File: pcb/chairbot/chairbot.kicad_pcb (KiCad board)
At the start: 2 copper layers, 66.9 x 100 mm, 35 parts, among them J1 Conn_01x02, J2 Conn_01x05, J3 Conn_01x02, J4 Conn_01x07, J5 Conn_01x07, Q1 ZXMN4A06G, U1 ESP32mini, U2 74HCT08, U3 74HCT244, U4 buck-converter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

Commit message: Fix various issues.
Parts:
- removed F1: Fuse, Resistor_THT:R_Axial_DIN0309_L9.0mm_D3.2mm_P2.54mm_Vertical
- added C11: 100n, Capacitor_SMD:C_0603_1608Metric, F.Cu at (71.8, 137.8)
- added R3: 10K, Resistor_SMD:R_0603_1608Metric, F.Cu at (56.5, 151.1)
- added R4: 1K, Resistor_SMD:R_0603_1608Metric, F.Cu at (71.8, 141.0)
- added R5: 2K2, Resistor_SMD:R_0603_1608Metric, F.Cu at (59.1, 90.8)
- added REF**: MountingHole_3.2mm_M3, MountingHole:MountingHole_3.2mm_M3, F.Cu at (97.2, 138.7)
- moved D1 11.9 mm to (51.2, 176.5), turned to 0 degrees
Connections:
- D1 pad 2: GND -> Net-(D1-Pad2)
- J1 pad 2: Net-(F1-Pad2) -> Net-(D1-Pad2)
- J4 pad 6: (no net) -> Net-(J4-Pad6)
- J5 pad 6: (no net) -> Net-(J5-Pad6)
- U1 pad 13: (no net) -> Net-(U1-Pad13)
- U1 pad 15: (no net) -> Net-(U1-Pad15)
- U1 pad 17: (no net) -> Net-(U1-Pad17)
- U1 pad 18: (no net) -> Net-(U1-Pad18)
- U1 pad 19: (no net) -> Net-(U1-Pad19)
- U1 pad 2: (no net) -> Net-(U1-Pad2)
- U1 pad 20: (no net) -> Net-(U1-Pad20)
- U1 pad 21: (no net) -> Brake
- U1 pad 23: (no net) -> Net-(U1-Pad23)
- U1 pad 24: (no net) -> MISO
- U1 pad 26: Brake -> Vbat
- U1 pad 3: (no net) -> Net-(U1-Pad3)
- U1 pad 34: MISO -> Net-(U1-Pad34)
- U1 pad 37: (no net) -> Net-(U1-Pad37)
- U1 pad 38: (no net) -> Net-(U1-Pad38)
- U1 pad 39: (no net) -> Net-(U1-Pad39)
- U1 pad 4: (no net) -> Net-(U1-Pad4)
- U1 pad 40: (no net) -> Net-(U1-Pad40)
- U1 pad 5: (no net) -> Net-(U1-Pad5)
- U2 pad 11: (no net) -> Net-(U2-Pad11)
- U2 pad 6: (no net) -> Net-(U2-Pad6)
- U2 pad 8: (no net) -> Net-(U2-Pad8)
- U3 pad 3: (no net) -> Net-(U3-Pad3)
- U3 pad 5: (no net) -> Net-(U3-Pad5)
- U3 pad 7: (no net) -> Net-(U3-Pad7)
- U3 pad 9: (no net) -> Net-(U3-Pad9)
- U5 pad 8: (no net) -> Net-(U5-Pad8)
- U9 pad 5: (no net) -> Net-(U9-Pad5)
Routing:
- net Vbat: track 0.00 -> 85.8 mm, vias 0 -> 5
- net MISO: track 51.3 -> 79.2 mm, vias 0 -> 1
- net Net-(F1-Pad2): track 11.8 -> 0.00 mm
- net Net-(D1-Pad2): track 0.00 -> 7.44 mm
- net +5V: track 250.2 -> 253.9 mm
- net GND: track 364.2 -> 366.8 mm
- net Brake: track 148.3 -> 145.8 mm
- net EN: track 20.6 -> 22.9 mm
- net +24V: track 79.5 -> 77.5 mm

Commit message: Fix more stuff.
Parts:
- moved R1 1.27 mm to (77.5, 177.8)
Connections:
- Q1 pad 1: Net-(D2-Pad2) -> Net-(Q1-Pad1)
- Q1 pad 2: Net-(Q1-Pad2) -> Net-(D2-Pad2)
- R1 pad 1: Net-(Q1-Pad2) -> Net-(Q1-Pad1)
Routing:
- net Net-(Q1-Pad1): track 0.00 -> 8.70 mm, vias 0 -> 2
- net Net-(Q1-Pad2): track 7.62 -> 0.00 mm
- net GND: track 366.8 -> 364.3 mm
- net Net-(D2-Pad2): track 32.3 -> 30.3 mm
- net Brake: track 145.8 -> 144.5 mm
- added copper zone on F.Cu, net GND

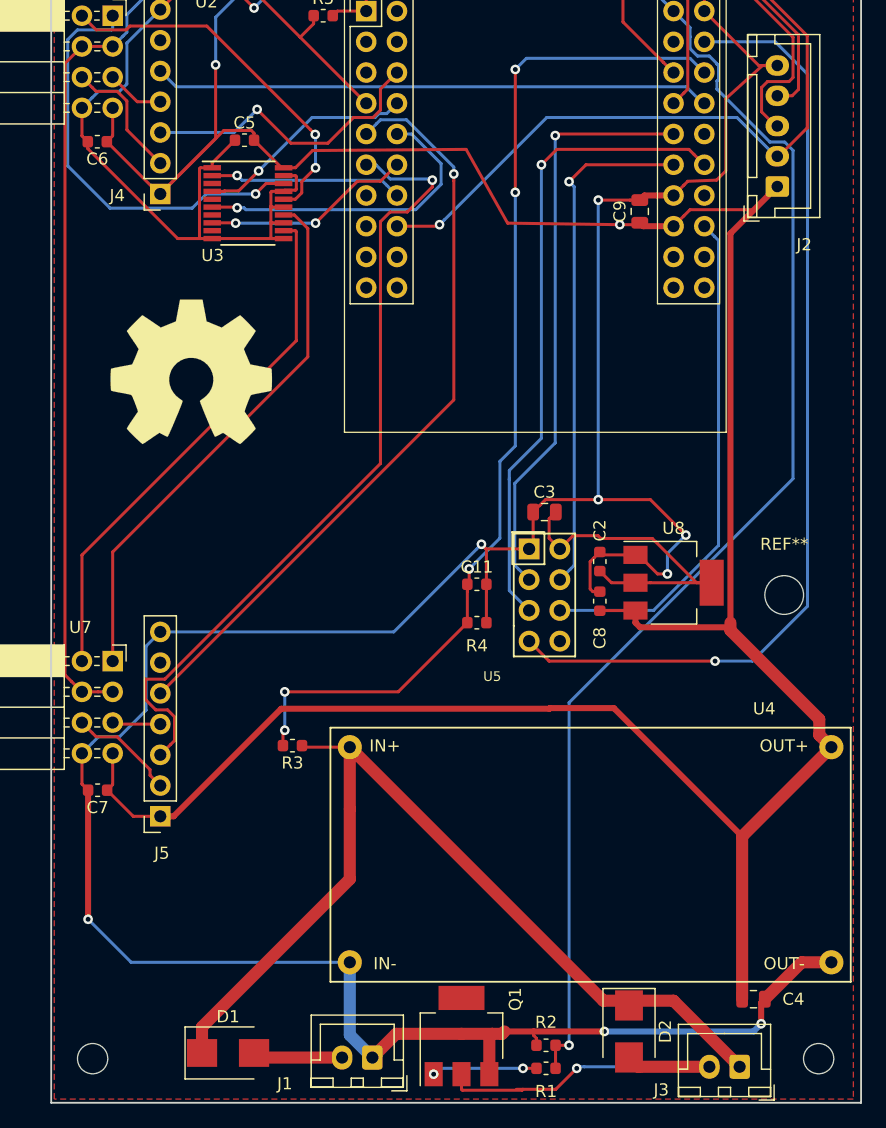
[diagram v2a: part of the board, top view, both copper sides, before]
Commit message: Tweak pin numbers.
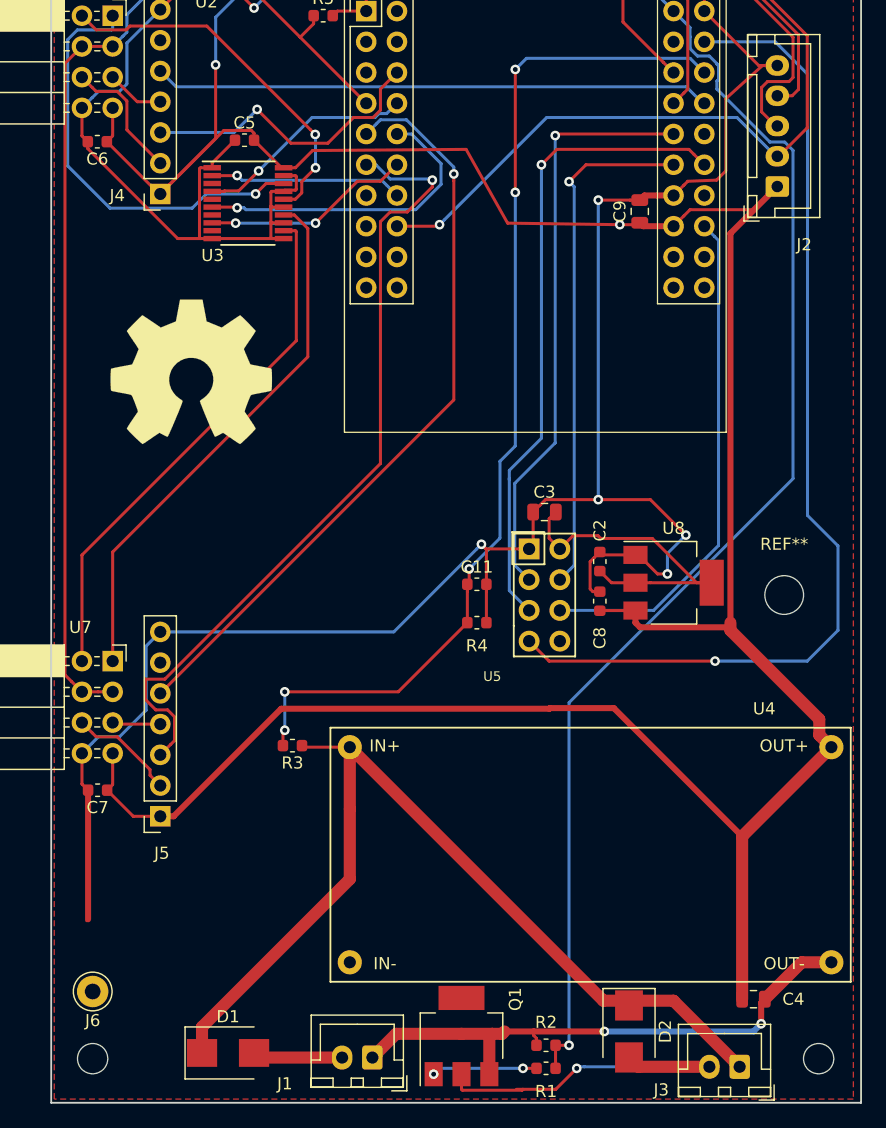
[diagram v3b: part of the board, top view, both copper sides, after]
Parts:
- added J6: GND, Connector_Pin:Pin_D1.3mm_L11.0mm, F.Cu at (40.0, 171.4)
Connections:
- R1 pad 2: Brake -> EN
- R2 pad 2: Brake -> EN
- U1 pad 21: Brake -> Net-(U1-Pad21)
- U1 pad 26: Vbat -> EN
- U1 pad 7: EN -> Vbat
- U2 pad 2: Brake -> EN
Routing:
- net GND: track 364.3 -> 332.5 mm, vias 8 -> 7
- net MISO: track 79.2 -> 83.9 mm
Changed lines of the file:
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@@
-(kicad_pcb (version 20171130) (host pcbnew 5.0.2-bee76a0~70~ubuntu18.04.1)
+(kicad_pcb (version 20171130) (host pcbnew 5.1.2-f72e74a~84~ubuntu18.04.1)
   (general
     (thickness 1.6)
     (drawings 5)
-    (tracks 550)
+    (tracks 547)
     (zones 0)
-    (modules 39)
-    (nets 65)
+    (modules 40)
+    (nets 66)
   )
   (page A4)
   (layers
-    (0 F.Cu signal)
+    (0 F.Cu signal hide)
     (31 B.Cu signal)
     (32 B.Adhes user)
@@
   )
   (setup
-    (last_trace_width 1)
+    (last_trace_width 0.25)
     (user_trace_width 0.5)
     (user_trace_width 1)
@@
     (zone_45_only no)
     (trace_min 0.2)
-    (segment_width 0.2)
-    (edge_width 0.15)
     (via_size 0.8)
     (via_drill 0.4)
@@
     (uvia_min_size 0.2)
     (uvia_min_drill 0.1)
+    (edge_width 0.15)
+    (segment_width 0.2)
     (pcb_text_width 0.3)
     (pcb_text_size 1.5 1.5)
@@
       (padsonsilk false)
       (subtractmaskfromsilk false)
-      (outputformat 5)
+      (outputformat 1)
       (mirror false)
       (drillshape 0)
@@
   (net 63 "Net-(D1-Pad2)")
   (net 64 "Net-(Q1-Pad1)")
+  (net 65 "Net-(U1-Pad21)")
   (net_class Default "This is the default net class."
     (clearance 0.2)
@@
     (add_net "Net-(U1-Pad2)")
     (add_net "Net-(U1-Pad20)")
+    (add_net "Net-(U1-Pad21)")
     (add_net "Net-(U1-Pad23)")
     (add_net "Net-(U1-Pad3)")
@@
       (net 25 SDA0))
     (pad 26 thru_hole oval (at 27.94 5.08) (size 1.7 1.7) (drill 1) (layers *.Cu *.Mask)
-      (net 35 Vbat))
+      (net 22 EN))
     (pad 25 thru_hole oval (at 25.4 5.08) (size 1.7 1.7) (drill 1) (layers *.Cu *.Mask)
       (net 26 SCL0))
@@
       (net 1 GND))
     (pad 21 thru_hole oval (at 25.4 0) (size 1.7 1.7) (drill 1) (layers *.Cu *.Mask)
-      (net 5 Brake))
+      (net 65 "Net-(U1-Pad21)"))
     (pad 20 thru_hole oval (at 2.54 22.86) (size 1.7 1.7) (drill 1) (layers *.Cu *.Mask)
       (net 44 "Net-(U1-Pad20)"))
@@
       (net 21 IO18))
     (pad 7 thru_hole oval (at 0 7.62) (size 1.7 1.7) (drill 1) (layers *.Cu *.Mask)
-      (net 22 EN))
+      (net 35 Vbat))
     (pad 6 thru_hole oval (at 2.54 5.08) (size 1.7 1.7) (drill 1) (layers *.Cu *.Mask)
       (net 32 IS_A_L_P))
@@
     (fp_line (start -0.8 0.4) (end -0.8 -0.4) (layer F.Fab) (width 0.1))
     (pad 2 smd roundrect (at 0.7875 0) (size 0.875 0.95) (layers F.Cu F.Paste F.Mask) (roundrect_rratio 0.25)
-      (net 5 Brake))
+      (net 22 EN))
     (pad 1 smd roundrect (at -0.7875 0) (size 0.875 0.95) (layers F.Cu F.Paste F.Mask) (roundrect_rratio 0.25)
       (net 64 "Net-(Q1-Pad1)"))
@@
       (net 1 GND))
     (pad 2 smd roundrect (at 0.7875 0) (size 0.875 0.95) (layers F.Cu F.Paste F.Mask) (roundrect_rratio 0.25)
-      (net 5 Brake))
+      (net 22 EN))
     (model ${KISYS3DMOD}/Resistor_SMD.3dshapes/R_0603_1608Metric.wrl
       (at (xyz 0 0 0))
@@
       (net 22 EN))
     (pad 2 smd rect (at -2.95 -1.3) (size 1.45 0.45) (layers F.Cu F.Paste F.Mask)
-      (net 5 Brake))
+      (net 22 EN))
     (pad 3 smd rect (at -2.95 -0.65) (size 1.45 0.45) (layers F.Cu F.Paste F.Mask)
       (net 6 "Net-(U2-Pad3)"))
@@
     )
   )
+  (module Connector_Pin:Pin_D1.3mm_L11.0mm (layer F.Cu)
+    (at 40.005 171.45)
+    (descr "solder Pin_ diameter 1.3mm, hole diameter 1.3mm, length 11.0mm")
+    (tags "solder Pin_ pressfit")
+    (fp_text reference J6 (at 0 2.4) (layer F.SilkS)
+      (effects (font (size 1 1) (thickness 0.15)))
+    )
+    (fp_text value GND (at 0 -2.05) (layer F.Fab)
+      (effects (font (size 1 1) (thickness 0.15)))
+    )
+    (fp_text user %R (at 0 2.4) (layer F.Fab)
+      (effects (font (size 1 1) (thickness 0.15)))
+    )
+    (fp_circle (center 0 0) (end 1.8 0) (layer F.CrtYd) (width 0.05))
+    (fp_circle (center 0 0) (end 0.65 -0.05) (layer F.Fab) (width 0.12))
+    (fp_circle (center 0 0) (end 1.25 -0.05) (layer F.Fab) (width 0.12))
+    (fp_circle (center 0 0) (end 1.6 0.05) (layer F.SilkS) (width 0.12))
+    (pad 1 thru_hole circle (at 0 0) (size 2.6 2.6) (drill 1.3) (layers *.Cu *.Mask)
+      (net 1 GND))
+    (model ${KISYS3DMOD}/Connector_Pin.3dshapes/Pin_D1.3mm_L11.0mm.wrl
+      (at (xyz 0 0 0))
+      (scale (xyz 1 1 1))
+      (rotate (xyz 0 0 0))
+    )
+  )
   (gr_text https://github.com/bullestock/chairbot/ (at 72.517 107.696 90) (layer B.SilkS)
     (effects (font (size 1.5 1.5) (thickness 0.3)) (justify mirror))
@@
   (segment (start 76.4055 134.5415) (end 76.073 134.874) (width 0.25) (layer F.Cu) (net 1))
   (segment (start 76.4055 131.826) (end 76.4055 134.5415) (width 0.25) (layer F.Cu) (net 1))
-  (segment (start 61.253 175.045) (end 63.119 176.911) (width 1) (layer B.Cu) (net 1))
-  (segment (start 61.253 169.037) (end 61.253 175.045) (width 1) (layer B.Cu) (net 1))
   (segment (start 98.6005 169.037) (end 95.5525 172.085) (width 1) (layer F.Cu) (net 1))
   (segment (start 101.053 169.037) (end 98.6005 169.037) (width 1) (layer F.Cu) (net 1))
@@
   (via (at 81.788 130.80099) (size 0.8) (drill 0.4) (layers F.Cu B.Cu) (net 1))
   (segment (start 81.788 106.045) (end 81.788 130.80099) (width 0.25) (layer B.Cu) (net 1))
-  (segment (start 43.18 169.037) (end 61.253 169.037) (width 0.25) (layer B.Cu) (net 1) (status 800000))
-  (segment (start 39.624 165.481) (end 43.18 169.037) (width 0.25) (layer B.Cu) (net 1))
-  (via (at 39.624 165.481) (size 0.8) (drill 0.4) (layers F.Cu B.Cu) (net 1))
   (segment (start 39.506 165.599) (end 39.624 165.481) (width 0.25) (layer F.Cu) (net 1))
   (segment (start 72.5425 138.37) (end 72.5425 140.97) (width 0.25) (layer F.Cu) (net 1))
@@
   (segment (start 62.611 90.424) (end 60.2235 90.424) (width 0.25) (layer F.Cu) (net 1))
   (segment (start 39.624 165.481) (end 39.624 154.813) (width 0.5) (layer F.Cu) (net 1))
+  (segment (start 73.844009 174.948991) (end 74.041 174.752) (width 1) (layer F.Cu) (net 1))
+  (segment (start 63.119 176.911) (end 65.081009 174.948991) (width 1) (layer F.Cu) (net 1))
+  (segment (start 65.081009 174.948991) (end 70.485 174.948991) (width 1) (layer F.Cu) (net 1))
+  (segment (start 72.785 175.188991) (end 73.025 174.948991) (width 1) (layer F.Cu) (net 1))
+  (segment (start 72.785 178.283) (end 72.785 175.188991) (width 1) (layer F.Cu) (net 1))
+  (segment (start 70.485 174.948991) (end 73.025 174.948991) (width 1) (layer F.Cu) (net 1))
+  (segment (start 73.025 174.948991) (end 73.844009 174.948991) (width 1) (layer F.Cu) (net 1))
   (segment (start 41.656 100.7365) (end 41.1735 101.219) (width 0.25) (layer F.Cu) (net 2))
   (segment (start 41.656 98.425) (end 41.656 100.7365) (width 0.25) (layer F.Cu) (net 2))
@@
   (segment (start 80.645 177.673) (end 90.972 177.673) (width 0.25) (layer B.Cu) (net 4) (status 800000))
   (segment (start 70.485 178.283) (end 70.485 178.533) (width 0.25) (layer F.Cu) (net 4))
-  (segment (start 73.844009 174.948991) (end 74.041 174.752) (width 1) (layer F.Cu) (net 1))
-  (segment (start 63.119 176.911) (end 65.081009 174.948991) (width 1) (layer F.Cu) (net 1))
-  (segment (start 65.081009 174.948991) (end 70.485 174.948991) (width 1) (layer F.Cu) (net 1))
-  (segment (start 72.785 175.188991) (end 73.025 174.948991) (width 1) (layer F.Cu) (net 1))
-  (segment (start 72.785 178.283) (end 72.785 175.188991) (width 1) (layer F.Cu) (net 1))
-  (segment (start 70.485 174.948991) (end 73.025 174.948991) (width 1) (layer F.Cu) (net 1))
-  (segment (start 73.025 174.948991) (end 73.844009 174.948991) (width 1) (layer F.Cu) (net 1))
   (via (at 80.01 177.8) (size 0.8) (drill 0.4) (layers F.Cu B.Cu) (net 4))
   (segment (start 80.645 177.673) (end 80.137 177.673) (width 0.25) (layer B.Cu) (net 4))
@@
   (segment (start 91.753081 92.964) (end 90.551 92.964) (width 0.25) (layer B.Cu) (net 14))
   (segment (start 96.410715 92.964) (end 91.753081 92.964) (width 0.25) (layer B.Cu) (net 14))
+  (segment (start 99.06 144.145) (end 101.6 141.605) (width 0.25) (layer B.Cu) (net 14))
+  (segment (start 91.44 144.145) (end 99.06 144.145) (width 0.25) (layer B.Cu) (net 14))
+  (segment (start 101.6 141.605) (end 101.6 134.62) (width 0.25) (layer B.Cu) (net 14))
   (segment (start 99.080001 95.633286) (end 96.410715 92.964) (width 0.25) (layer B.Cu) (net 14))
-  (segment (start 94.543002 144.145) (end 99.080001 139.608001) (width 0.25) (layer B.Cu) (net 14))
-  (segment (start 99.080001 139.608001) (end 99.080001 95.633286) (width 0.25) (layer B.Cu) (net 14))
-  (segment (start 91.44 144.145) (end 94.543002 144.145) (width 0.25) (layer B.Cu) (net 14))
+  (segment (start 101.6 134.62) (end 99.080001 132.100001) (width 0.25) (layer B.Cu) (net 14))
+  (segment (start 99.080001 132.100001) (end 99.080001 95.633286) (width 0.25) (layer B.Cu) (net 14))
   (segment (start 76.073 139.954) (end 74.434388 138.315388) (width 0.25) (layer B.Cu) (net 15))
   (segment (start 74.434388 129.159) (end 74.434388 128.384612) (width 0.25) (layer B.Cu) (net 15))

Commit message: Update.
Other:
- net class Default removed

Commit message: Add missing files.
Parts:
- removed C2, C5, C8: 100n, Capacitor_SMD:C_0603_1608Metric
- removed C3: 10u, Capacitor_SMD:C_0805_2012Metric
- removed REF** (x4): MountingHole_2.5mm, MountingHole:MountingHole_2.5mm
- removed REF**: OSHW-Symbol_13.4x12mm_SilkScreen, Symbol:OSHW-Symbol_13.4x12mm_SilkScreen
- removed REF**: MountingHole_3.2mm_M3, MountingHole:MountingHole_3.2mm_M3
- removed U2: 74HCT08, Package_SO:TSSOP-14_4.4x5mm_P0.65mm
- removed U5: nRF24L01+, chairbot:nRF24L01
- removed U8: AMS1117-3.3, Package_TO_SOT_SMD:SOT-223-3_TabPin2
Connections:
- J4 pad 6: Net-(J4-Pad6) -> unconnected-(J4-Pin_6-Pad6)
- J5 pad 6: Net-(J5-Pad6) -> unconnected-(J5-Pin_6-Pad6)
- U1 pad 13: Net-(U1-Pad13) -> unconnected-(U1-TMS-Pad13)
- U1 pad 15: Net-(U1-Pad15) -> unconnected-(U1-NC-Pad15)
- U1 pad 17: Net-(U1-Pad17) -> unconnected-(U1-TCK-Pad17)
- U1 pad 18: Net-(U1-Pad18) -> unconnected-(U1-SD2-Pad18)
- U1 pad 19: Net-(U1-Pad19) -> unconnected-(U1-SD3-Pad19)
- U1 pad 2: Net-(U1-Pad2) -> unconnected-(U1-RST-Pad2)
- U1 pad 20: Net-(U1-Pad20) -> unconnected-(U1-CMD-Pad20)
- U1 pad 21: Net-(U1-Pad21) -> unconnected-(U1-U0TXD-Pad21)
- U1 pad 23: Net-(U1-Pad23) -> unconnected-(U1-U0RXD-Pad23)
- U1 pad 3: Net-(U1-Pad3) -> unconnected-(U1-NC-Pad3)
- U1 pad 34: Net-(U1-Pad34) -> unconnected-(U1-IO0-Pad34)
- U1 pad 37: Net-(U1-Pad37) -> unconnected-(U1-TD0-Pad37)
- U1 pad 38: Net-(U1-Pad38) -> unconnected-(U1-SD1-Pad38)
- U1 pad 39: Net-(U1-Pad39) -> unconnected-(U1-SD0-Pad39)
- U1 pad 4: Net-(U1-Pad4) -> unconnected-(U1-SENSOR_VP-Pad4)
- U1 pad 40: Net-(U1-Pad40) -> unconnected-(U1-CLK-Pad40)
- U1 pad 5: Net-(U1-Pad5) -> unconnected-(U1-SENSOR_VN-Pad5)
- U3 pad 17: GND -> EN
- U3 pad 3: Net-(U3-Pad3) -> EN5
- U3 pad 5: Net-(U3-Pad5) -> unconnected-(U3-2Y1-Pad5)
- U3 pad 7: Net-(U3-Pad7) -> unconnected-(U3-2Y2-Pad7)
- U3 pad 9: Net-(U3-Pad9) -> unconnected-(U3-2Y3-Pad9)
- U6 pad 3: Net-(U2-Pad3) -> EN5
- U6 pad 4: Net-(U2-Pad3) -> EN5
- U7 pad 3: Net-(U2-Pad3) -> EN5
- U7 pad 4: Net-(U2-Pad3) -> EN5
- U9 pad 5: Net-(U9-Pad5) -> unconnected-(U9-EN-Pad5)
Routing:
- net EN: track 22.9 -> 167.4 mm, vias 0 -> 2
- net Brake: track 144.5 -> 0.00 mm, vias 2 -> 0
- net Net-(U2-Pad3): track 72.1 -> 0.00 mm, vias 1 -> 0
- net EN5: track 0.00 -> 72.1 mm, vias 0 -> 1
- net Net-(C2-Pad2): track 27.9 -> 0.00 mm
- net (no net): track 0.00 -> 27.9 mm
